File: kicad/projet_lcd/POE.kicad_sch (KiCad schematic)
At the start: 63 parts, among them Q1 FOD817A3SD, T1 749119950, U4 SI3404-A-GMR, U5 TLV431, U6 AMS1117-3.3

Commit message: migrating POE.kicad_sch to new lib. TBC
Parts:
- removed C20, C25: 100nF, symbol Generiques:C
- removed C21: 12uF, symbol Generiques:C_Polarized
- removed C22, C23, C27: 1uF, symbol Generiques:C
- removed C24, C26: 10nF, symbol Generiques:C
- removed C33, C34, C36: NI, symbol Generiques:C
- removed C37: 1.5nF, symbol Generiques:C
- removed C38: 1nF, symbol Generiques:C
- removed C39: 22uF, symbol Generiques:C_Polarized
- removed C40: 10uF, symbol Generiques:C_Polarized
- removed D3: S1B, symbol Generiques:D
- removed D4: 1N4148W, symbol Generiques:D
- removed D6: LED, symbol Generiques:LED
- removed FB3: 700 Ohms @150MHz, symbol Generiques:FerriteBead
- removed R25: 3R, symbol Generiques:R
- removed R26: 48R7, symbol Generiques:R
- removed R27: 0R62, symbol Generiques:R
- removed R28: 24K3, symbol Generiques:R
- removed R29: 88K7, symbol Generiques:R
- removed R30: 82K, symbol Generiques:R
- removed R31, R39: 0R, symbol Generiques:R
- removed R34: 4K7, symbol Generiques:R
- removed R35: NI, symbol Generiques:R
- removed R36: 750R, symbol Generiques:R
- removed R37: 36K5, symbol Generiques:R
- removed R38: 12K1, symbol Generiques:R
- removed R40: 10R, symbol Generiques:R
- removed R41: 1K, symbol Generiques:R
- removed TP1, TP11, TP2, TP3, TP4, TP5, TP6, TP7, TP8, TP9: ~, symbol PCB_Utils:Test_point
- removed U5: TLV431, symbol Generiques:Vref
- added C20: 10uF, symbol Generics:C_Polarized
- added C21: 12uF, symbol Generics:C_Polarized
- added C22, C36: 100nF, symbol Generics:C
- added C23: 22uF, symbol Generics:C_Polarized
- added C25, C27: 10nF, symbol Generics:C
- added C26, C60, C61: 1uF, symbol Generics:C
- added C33, C34, C38: NI, symbol Generics:C
- added C37: 1nF, symbol Generics:C
- added C59: 1.5nF, symbol Generics:C
- added D3, D7: ~, symbol Generics:D
- added D6: ~, symbol Generics:D_LED
- added FB3: 700 Ohms @150MHz, symbol Generics:FB
- added R26: 48R7, symbol Generics:R
- added R27: 3R, symbol Generics:R
- added R28: 24K3, symbol Generics:R
- added R29: 0R62, symbol Generics:R
- added R30, R38: 0R, symbol Generics:R
- added R31: 88K7, symbol Generics:R
- added R34: 82K, symbol Generics:R
- added R35: NI, symbol Generics:R
- added R36: 12K1, symbol Generics:R
- added R37: 750R, symbol Generics:R
- added R39: 4K7, symbol Generics:R
- added R40: 10R, symbol Generics:R
- added R41: 1K, symbol Generics:R
- added R43: 36K5, symbol Generics:R
- added TP09, TP1, TP2, TP3, TP4, TP5, TP6, TP7, TP8: ~, symbol PCB_Utils:TP
- added U8: ~, symbol Voltage_Regulators:TL431
- C28, C29, C30, C32, C35: symbol Generiques:C -> Generics:C
- C31: symbol Generiques:C_Polarized -> Generics:C_Polarized
- D5: symbol Generiques:D_Schottky -> Generics:D_Schottky
- FB2: symbol Generiques:FerriteBead -> Generics:FB
- L1: symbol Generiques:L -> Generics:L
- Q1: symbol Generiques:Optocoupler -> Generics:OP; Part# (none) -> NI
- R32, R33: symbol Generiques:R -> Generics:R
- TP10: symbol PCB_Utils:Test_point -> PCB_Utils:TP
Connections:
- net +3.3V: now also C23.P
- net +5V: now also C31.P, C32.2, C35.2, R33.1, C20.P, C33.2, C34.2, R40.2 (1), R41.2 (1), TP8.1; no longer C31.1, C32.1, C35.1, R33.2
- net GND: now also C29.1, C30.1, C31.N, C32.1, C35.1, C20.N, C23.N, C33.1, C34.1, C37.2, D6.K, R36.2 (1), TP09.1, U8.2 (A); no longer C29.2, C30.2, C31.2, C32.2, C35.2
- net vneg: now also C22.1, FB3.2, R26.1, TP2.1
- net vpos: now also C21.P, C25.2, C27.2, C60.2, C61.2, R27.2 (1), R28.2 (1), R31.2 (1), R34.2 (1), TP1.1
- net vss: now also C21.N, C26.1, C27.1, C36.1, C37.1, C38.1, C60.1, C61.1, R29.1, TP3.1
- net at T1.2: now also R30.2 (1)
- net at T1.3, U4.18 (SWO): now also D7.A, TP4.1
- net at T1.7, T1.8: now also C28.2, D5.A; no longer C28.1, D5.2 (A)
- net at U4.5 (VDD): now also C36.2, R39.2 (1)
- net at Q1.C, U4.3 (EROUT): now also R35.2 (1), R39.1, TP6.1
- net at U4.16 (VT15): now also C26.2, D3.K, TP5.1
- net at R32.1: now also C29.2, C30.2, D5.K, L1.1, R33.2 (1); no longer C28.2
- net at U4.1 (ISNS), U4.8 (HSO): now also R29.2 (1)
- net at U4.10 (RFREQ): now also R31.1
- net at D1.4 (DC_P), D2.4 (DC_P): now also FB3.1
- net at U4.6 (RDET): now also R28.1
- net at U4.9 (RCL): now also R26.2 (1)
- new net: R37.2 (1), R40.1, R43.2 (1), TP7.1
- new net: D3.A, R30.1
- new net: C25.1, D7.K, R34.1
- new net: D6.A, R41.1
- new net: C28.1, R32.2 (1)
- new net: Q1.A, R37.1
- new net: C59.1, Q1.K, U8.1 (K)
- new net: C38.2, R35.1
- new net: C22.2, R27.1
- new net: C59.2, R38.1
- new net: R36.1, R38.2 (1), R43.1, U8.1 (K)
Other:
- moved on the sheet: C28, C29, C30, C32, C35, D5, L1

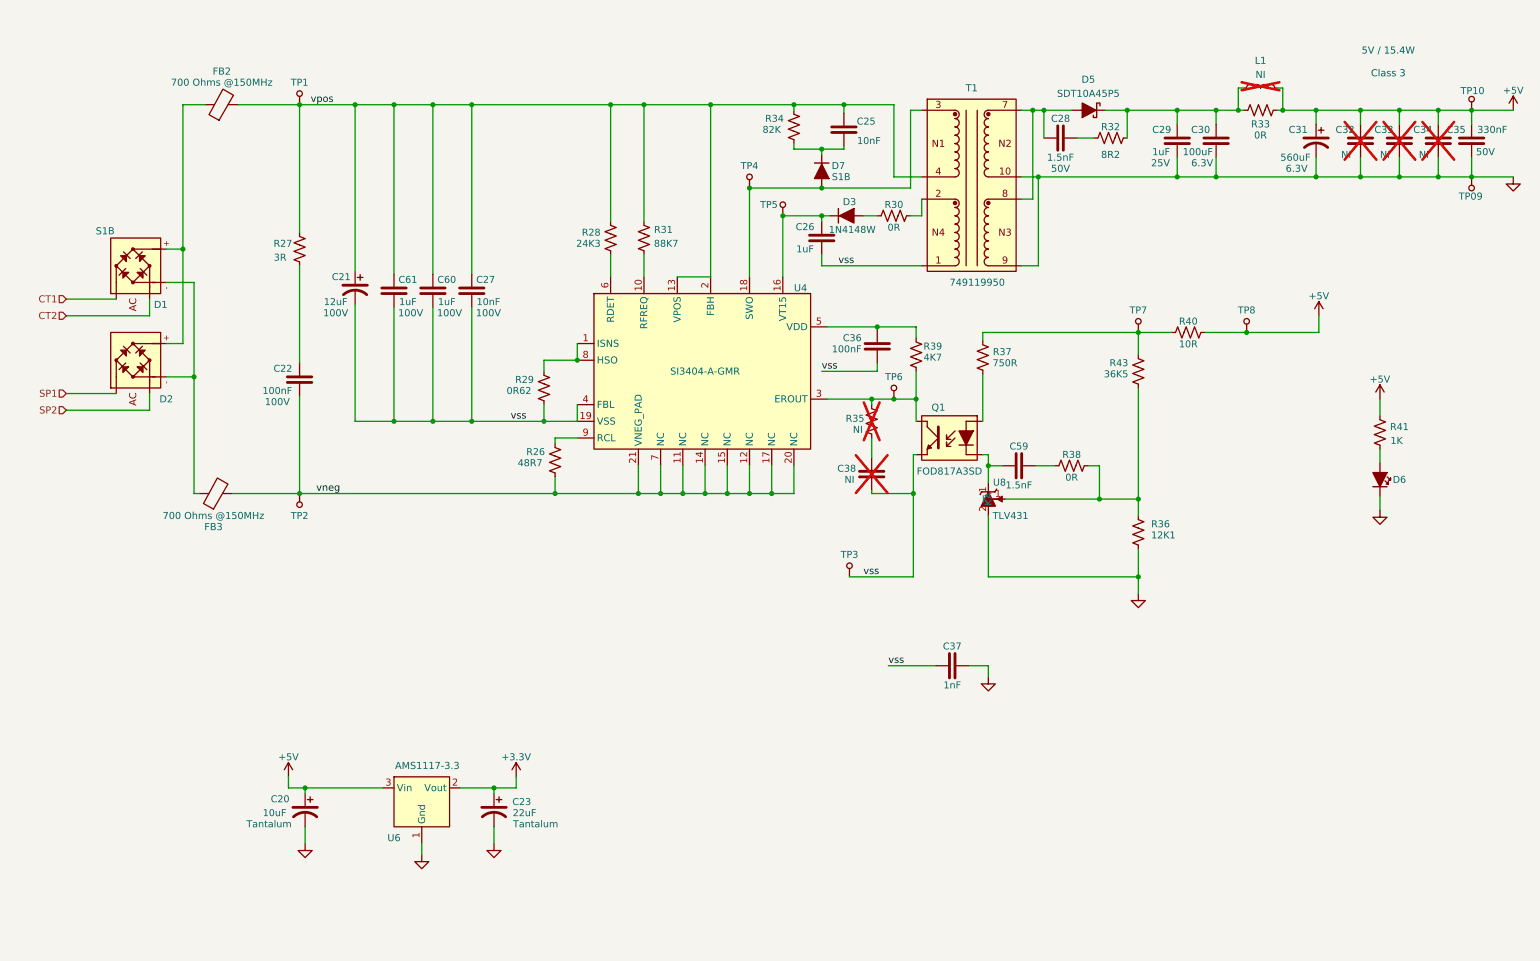
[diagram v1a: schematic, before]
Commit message: Done with POE.kicad_sch migration
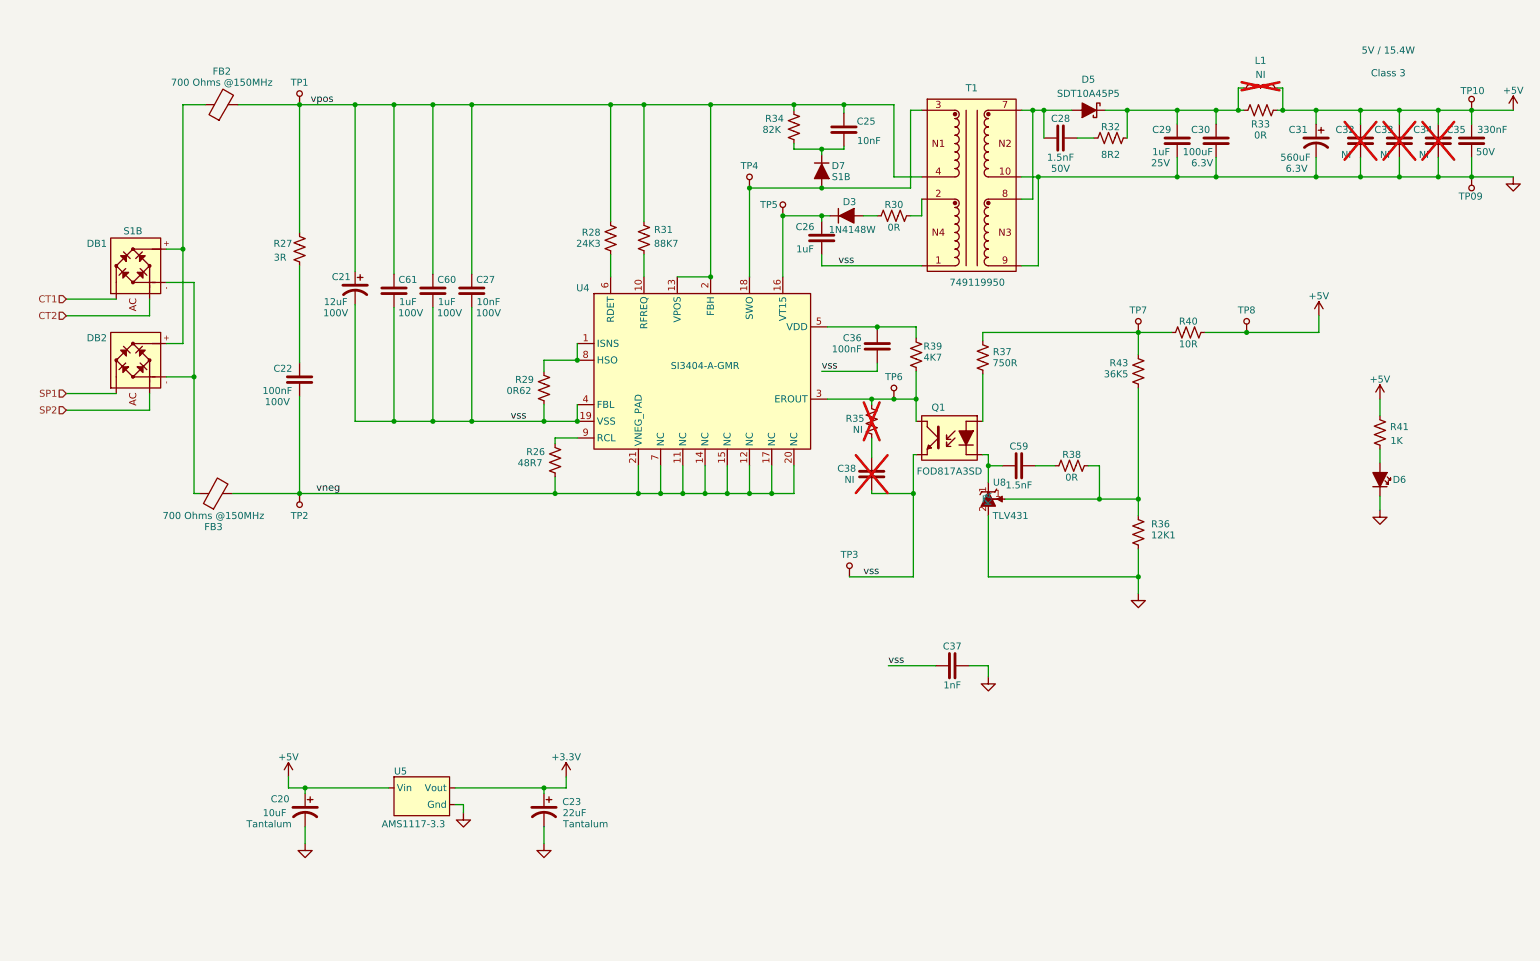
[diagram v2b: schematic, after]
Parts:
- removed D1, D2: ~, symbol Diodes:Diode_bridge
- removed U6: AMS1117-3.3, symbol LDO:AMS1117-3.3
- added DB1, DB2: ~, symbol Generics:DB
- added U5: ~, symbol Voltage_Regulators:AMS1117-3.3
- U4: value SI3404-A-GMR -> ~; symbol Chips:SI3404-A-GMR_ -> Ethernet:SI3404-A-GMR; LCSC Part # (none) -> C461934; Part# (none) -> SI3404-A-GMR
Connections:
- net +3.3V: now also U5.Vout
- net +5V: now also U5.Vin
- net CT1: now also DB1.1 (AC)
- net CT2: now also DB1.2 (AC)
- net GND: now also U5.Gnd
- net SP1: now also DB2.1 (AC)
- net SP2: now also DB2.2 (AC)
- net at FB2.1: now also DB1.3 (DC_N), DB2.3 (DC_N)
- net at FB3.1: now also DB1.4 (DC_P), DB2.4 (DC_P)
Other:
- moved on the sheet: C23

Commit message: EOD
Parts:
- removed C36: 100nF, symbol Generics:C
- added C41: 100nF, Generics:C_0603, symbol Generics:C
- added TP11, TP12: ~, PCB_Utils:TP_1.5, symbol PCB_Utils:TP
- C19: renamed from C28; Tension 50V -> (none)
- C21: renamed from C29; Tension 25V -> (none)
- C22: renamed from C30; Tension 6.3V -> (none)
- C23: renamed from C31; Tension 6.3V -> (none)
- C27: renamed from C35; Tension 50V -> (none)
- C29: renamed from C21; Voltage 100V -> (none)
- C30: renamed from C61; Voltage 100V -> (none)
- C31: renamed from C60; Voltage 100V -> (none)
- C32: renamed from C27; Voltage 100V -> (none)
- C34: renamed from C22; Voltage 100V -> (none)
- C35: renamed from C59; footprint (none) -> Generics:C_0603; LCSC Part # (none) -> C1595
- C36: renamed from C38; footprint (none) -> Generics:C_0603
- C37: footprint (none) -> Generics:C_0603; LCSC Part # (none) -> C1588
- C38: renamed from C20; footprint (none) -> Generics:C_0603; symbol Generics:C_Polarized -> Generics:C; Comments Tantalum -> (none); LCSC Part # (none) -> C19702
- C39: renamed from C23; footprint (none) -> Generics:C_tantalum_A; LCSC Part #  (none) -> C129272
- D1: renamed from D5; Part# (none) -> NI
- D2: renamed from D7; Part# S1B -> NI
- D3: Part# 1N4148W -> NI
- D4: renamed from D6; footprint (none) -> Generics:D_LED_0603
- R10: renamed from R39; footprint (none) -> Generics:R_0402; LCSC Part # (none) -> C25900
- R11: renamed from R37; footprint (none) -> Generics:R_0402; LCSC Part # (none) -> C137936
- R12: renamed from R43; footprint (none) -> Generics:R_0402; LCSC Part # (none) -> C15011
- R14: renamed from R35; footprint (none) -> Generics:R_0603
- R15: renamed from R41; footprint (none) -> Generics:R_0603
- R16: renamed from R38; footprint (none) -> Generics:R_0603; LCSC Part # (none) -> C22864
- R18: renamed from R36; footprint (none) -> Generics:R_0402; LCSC Part # (none) -> C132157
- R9: renamed from R40; footprint (none) -> Generics:R_0402; LCSC Part # (none) -> C25077
- TP1: footprint (none) -> PCB_Utils:TP_1.5
- TP10: renamed from TP3; footprint (none) -> PCB_Utils:TP_1.5
- TP2: renamed from TP10; footprint (none) -> PCB_Utils:TP_1.5
- TP3: renamed from TP09; footprint (none) -> PCB_Utils:TP_1.5
- TP6: renamed from TP7; footprint (none) -> PCB_Utils:TP_1.5
- TP7: renamed from TP8; footprint (none) -> PCB_Utils:TP_1.5
- TP8: renamed from TP6; footprint (none) -> PCB_Utils:TP_1.5
- TP9: renamed from TP2; footprint (none) -> PCB_Utils:TP_1.5
- U3: renamed from U8; PART# TLV431 -> TL431
- renumbered C25 to C20, C32 to C24, C33 to C25, C34 to C26, C26 to C28, FB2 to FB1, FB3 to FB2, R29 to R13, R26 to R17, R33 to R2, R32 to R3, R34 to R4, R30 to R5, R28 to R6, R31 to R7, R27 to R8, U4 to U2, U5 to U4
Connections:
- net +3.3V: now also TP12.1
- net +5V: now also C38.2; no longer C38.P
- net GND: now also C38.1; no longer C38.N
- net vss: now also C41.1
- net at C21.2, C22.2, D1.K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: now also TP11.1
- net at C35.1, Q1.K: now also U3.K; no longer U3.1 (K)
- net at R10.2 (1), U2.5 (VDD): now also C41.2
- net at R12.1, R16.2 (1), R18.1: now also U3.Ref; no longer U3.1 (K)
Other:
- moved on the sheet: C27, C29, C30, C31, C32, C39, D4, R11, R12, R14, R15, R18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

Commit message: EOD
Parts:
- C19, C27: Comments (none) -> 50V
- C21: Comments (none) -> 25V
- C22, C23: Comments (none) -> 6.3V
- C29, C30, C31, C32, C34: Comments (none) -> 100V
- C39: LCSC Part # (none) -> C129272; LCSC Part #  C129272 -> (none)
- D2: Part# NI -> S1B
- D3: Part# NI -> 1N4148W
- TP4, TP5: footprint (none) -> PCB_Utils:TP_1.5
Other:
- moved on the sheet: C34
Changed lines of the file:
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@@
 	(wire
 		(pts
-			(xy 64 82) (xy 64 100)
+			(xy 64 79) (xy 64 100)
 		)
 		(stroke
@@
 	(wire
 		(pts
-			(xy 64 59) (xy 64 76)
+			(xy 64 59) (xy 64 73)
 		)
 		(stroke
@@
 			)
 		)
-		(property "Description" "Tranformer / PoE Size ER13 127uH 40mohm "
+		(property "Description" "Tranformer / PoE Size ER13 127uH 40mohm"
 			(at 207 14 0)
 			(effects
@@
 			)
 		)
+		(property "Cl" ""
+			(at 176 31 0)
+			(effects
+				(font
+					(size 1.27 1.27)
+				)
+			)
+		)
+		(property "ESR" ""
+			(at 176 31 0)
+			(effects
+				(font
+					(size 1.27 1.27)
+				)
+			)
+		)
+		(property "Precision" ""
+			(at 176 31 0)
+			(effects
+				(font
+					(size 1.27 1.27)
+				)
+			)
+		)
+		(property "REF" ""
+			(at 176 31 0)
+			(effects
+				(font
+					(size 1.27 1.27)
+				)
+			)
+		)
+		(property "Ref" ""
+			(at 176 31 0)
+			(effects
+				(font
+					(size 1.27 1.27)
+				)
+			)
+		)
+		(property "Tension" ""
+			(at 176 31 0)
+			(effects
+				(font
+					(size 1.27 1.27)
+				)
+			)
+		)
+		(property "Tolerance" ""
+			(at 176 31 0)
+			(effects
+				(font
+					(size 1.27 1.27)
+				)
+			)
+		)
+		(property "Type" ""
+			(at 176 31 0)
+			(effects
+				(font
+					(size 1.27 1.27)
+				)
+			)
+		)
 		(pin "10"
 		)
@@
 			)
 		)
-		(property "Part#" "NI"
+		(property "Part#" "1N4148W"
 			(at 164 52.5 0)
 			(do_not_autoplace yes)
@@
 			)
 		)
-		(property "Part#" "NI"
+		(property "Part#" "S1B"
 			(at 161.5 43 90)
 			(do_not_autoplace yes)
@@
 			)
 		)
-		(property "Comments" ""
-			(at 204 36 0)
+		(property "Comments" "50V"
+			(at 201 41.5 0)
 			(effects
 				(font
 					(size 1.25 1.25)
 				)
-				(hide yes)
 			)
 		)
@@
 			)
 		)
-		(property "Comments" ""
-			(at 229 39 0)
+		(property "Comments" "6.3V"
+			(at 226.5 40 90)
 			(effects
 				(font
 					(size 1.25 1.25)
 				)
-				(hide yes)
 			)
 		)
@@
 			)
 		)
-		(property "Comments" ""
-			(at 222 39 0)
+		(property "Comments" "25V"
+			(at 219 40 90)
 			(effects
 				(font
 					(size 1.25 1.25)
 				)
-				(hide yes)
 			)
 		)
@@
 			)
 		)
-		(property "Footprint" ""
+		(property "Footprint" "PCB_Utils:TP_1.5"
 			(at 145 43 0)
 			(effects
@@
 	(symbol
 		(lib_id "Generics:C")
-		(at 64 82 90)
+		(at 64 79 90)
 		(unit 1)
 		(exclude_from_sim no)
@@
 		(dnp no)
 		(property "Reference" "C34"
-			(at 61 77 90)
+			(at 61 74 90)
 			(do_not_autoplace yes)
 			(effects
@@
 		)
 		(property "Value" "100nF"
-			(at 60 81 90)
+			(at 60 78 90)
 			(do_not_autoplace yes)
 			(effects
@@
 		)
 		(property "Footprint" ""
-			(at 59.5348 77.69 90)
+			(at 59.5348 74.69 90)
 			(effects
 				(font
@@
 		)
 		(property "Datasheet" ""
-			(at 63.9 78.4 90)
+			(at 63.9 75.4 90)
 			(effects
 				(font
@@
 		)
 		(property "Description" "Unpolarized capacitor"
-			(at 73.6 79 0)
+			(at 73.6 76 0)
 			(effects
 				(font
@@
 		)
 		(property "Part#" ""
-			(at 64 82 0)
+			(at 64 79 0)
 			(effects
 				(font
@@
 			)
 		)
-		(property "Comments" ""
-			(at 64 82 0)
+		(property "Comments" "100V"
+			(at 60 80 90)
 			(effects
 				(font
 					(size 1.25 1.25)
 				)
-				(hide yes)
 			)
 		)
 		(property "LCSC Part #" ""
-			(at 64 82 0)
+			(at 64 79 0)
 			(effects
 				(font
@@
 			)
 		)
-		(property "Comments" ""
-			(at 74 65 0)
+		(property "Comments" "100V"
+			(at 70 67 90)
 			(effects
 				(font
 					(size 1.25 1.25)
 				)
-				(hide yes)
 			)
 		)
-		(property "LCSC Part # " ""
+		(property "LCSC Part #" ""
 			(at 74 65 0)
 			(effects
@@
 			)
 		)
-		(property "Comments" ""
-			(at 276 39 0)
+		(property "Comments" "50V"
+			(at 281 36 90)
 			(effects
 				(font
 					(size 1.25 1.25)
 				)
-				(hide yes)
 			)
 		)
@@
 			)
 		)
-		(property "Comments" ""
-			(at 89 65 0)
+		(property "Comments" "100V"
+			(at 92 66 90)
 			(effects
 				(font
 					(size 1.25 1.25)
 				)
-				(hide yes)
 			)
 		)
@@
 			)
 		)
-		(property "Comments" ""
-			(at 247 39 0)
+		(property "Comments" "6.3V"
+			(at 243.5 41 90)
 			(effects
 				(font
 					(size 1.25 1.25)
 				)
-				(hide yes)
 			)
 		)
-		(property "LCSC Part # " ""
+		(property "LCSC Part #" ""
 			(at 247 39 0)
 			(effects
@@
 			)
 		)
-		(property "LCSC Part # " "C129272"
+		(property "LCSC Part #" "C129272"
 			(at 103 160 0)
 			(effects
@@
 			)
 		)
-		(property "Comments" ""
-			(at 81 65 0)
+		(property "Comments" "100V"
+			(at 84 66 90)
 			(effects
 				(font
 					(size 1.25 1.25)
 				)
-				(hide yes)
 			)
 		)
@@
 			)
 		)
-		(property "Comments" ""
-			(at 97 65 0)
+		(property "Comments" "100V"
+			(at 100 66 90)
 			(effects
 				(font
 					(size 1.25 1.25)
 				)
-				(hide yes)
 			)
 		)
@@
 			)
 		)
-		(property "Footprint" ""
+		(property "Footprint" "PCB_Utils:TP_1.5"
 			(at 151 48 0)
 			(effects
